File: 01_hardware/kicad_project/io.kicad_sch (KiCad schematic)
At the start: 24 parts, among them J5 ADDR HDR, J6 PROG PADS, J7 ARM SWD 10, SW1 DIP-6

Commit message: Rev E BOM: in-stock LCSC first source for every part; 2nd/3rd sources checked
- First sources swapped (same footprints, layout unchanged): U1 STM32G474RBT3,
  Q2/Q3/Q5/Q6 NCEP068N10G, 10k 0402 FOJAN, 100n 0402 merged onto C307331,
  1u 0402 CCTC, R62/R63/R89/R82, FB1 Murata BLM18KG601SN1D, L2/L3 cjiang
  FNR5040S470MT, C82 KEMET C0G (was X7R), RS1 Milliohm HoJLR2512, SS110 MDD
- LCSC part numbers for the hand-soldered headers (J1-J5, J7, JP1)
- Schematic and PCB fields, BOM, JLC BOM/CPL, PDFs and design notes regenerated;
  netlist check 0 errors, DRC unchanged
- BOM_sourcing_revE.xlsx: live LCSC stock 2026-10-20, 2nd/3rd sources checked
  for pinout / land pattern / ratings, PCB reserve options for T2 and U9

Co-Authored-By: Claude Opus 5.5 <noreply@anthropic.com>
Claude-Session: https://claude.ai/code/session_01A35wrnwFKLPSaRSxxHs471
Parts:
- J5: LCSC (none) -> C42419913; MPN ADDR HDR -> PZ254V-11-06P-A40
- J7: LCSC (none) -> C41376037; MPN FTSH-105-01-L-DV-K or equiv. -> HX PZ1.27-2x5P TP
- R32, R33, R34, R35, R36, R37: LCSC C25744 -> C2906861
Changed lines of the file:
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@@
       (effects (font (size 1.27 1.27)) hide)
     )
-    (property "LCSC" "C25744" (id 4) (at 129.54 71.12 0)
+    (property "LCSC" "C2906861" (id 4) (at 129.54 71.12 0)
       (effects (font (size 1.27 1.27)) hide)
     )
@@
       (effects (font (size 1.27 1.27)) hide)
     )
-    (property "LCSC" "C25744" (id 4) (at 116.84 71.12 0)
+    (property "LCSC" "C2906861" (id 4) (at 116.84 71.12 0)
       (effects (font (size 1.27 1.27)) hide)
     )
@@
       (effects (font (size 1.27 1.27)) hide)
     )
-    (property "LCSC" "C25744" (id 4) (at 104.14 71.12 0)
+    (property "LCSC" "C2906861" (id 4) (at 104.14 71.12 0)
       (effects (font (size 1.27 1.27)) hide)
     )
@@
       (effects (font (size 1.27 1.27)) hide)
     )
-    (property "LCSC" "C25744" (id 4) (at 91.44 71.12 0)
+    (property "LCSC" "C2906861" (id 4) (at 91.44 71.12 0)
       (effects (font (size 1.27 1.27)) hide)
     )
@@
       (effects (font (size 1.27 1.27)) hide)
     )
-    (property "LCSC" "C25744" (id 4) (at 78.74 71.12 0)
+    (property "LCSC" "C2906861" (id 4) (at 78.74 71.12 0)
       (effects (font (size 1.27 1.27)) hide)
     )
@@
       (effects (font (size 1.27 1.27)) hide)
     )
-    (property "LCSC" "C25744" (id 4) (at 66.04 71.12 0)
+    (property "LCSC" "C2906861" (id 4) (at 66.04 71.12 0)
       (effects (font (size 1.27 1.27)) hide)
     )
@@
       (effects (font (size 1.27 1.27)) hide)
     )
-    (property "LCSC" "" (id 4) (at 96.52 157.48 0)
-      (effects (font (size 1.27 1.27)) hide)
-    )
-    (property "MPN" "ADDR HDR" (id 5) (at 96.52 157.48 0)
+    (property "LCSC" "C42419913" (id 4) (at 96.52 157.48 0)
+      (effects (font (size 1.27 1.27)) hide)
+    )
+    (property "MPN" "PZ254V-11-06P-A40" (id 5) (at 96.52 157.48 0)
       (effects (font (size 1.27 1.27)) hide)
     )
@@
       (effects (font (size 1.27 1.27)) hide)
     )
-    (property "LCSC" "" (id 4) (at 228.6 180.34 0)
-      (effects (font (size 1.27 1.27)) hide)
-    )
-    (property "MPN" "FTSH-105-01-L-DV-K or equiv." (id 5) (at 228.6 180.34 0)
-      (effects (font (size 1.27 1.27)) hide)
-    )
+    (property "LCSC" "C41376037" (id 4) (at 228.6 180.34 0)
+      (effects (font (size 1.27 1.27)) hide)
+    )
+    (property "MPN" "HX PZ1.27-2x5P TP" (id 5) (at 228.6 180.34 0)
+      (effects (font (size 1.27 1.27)) hide)
+    )

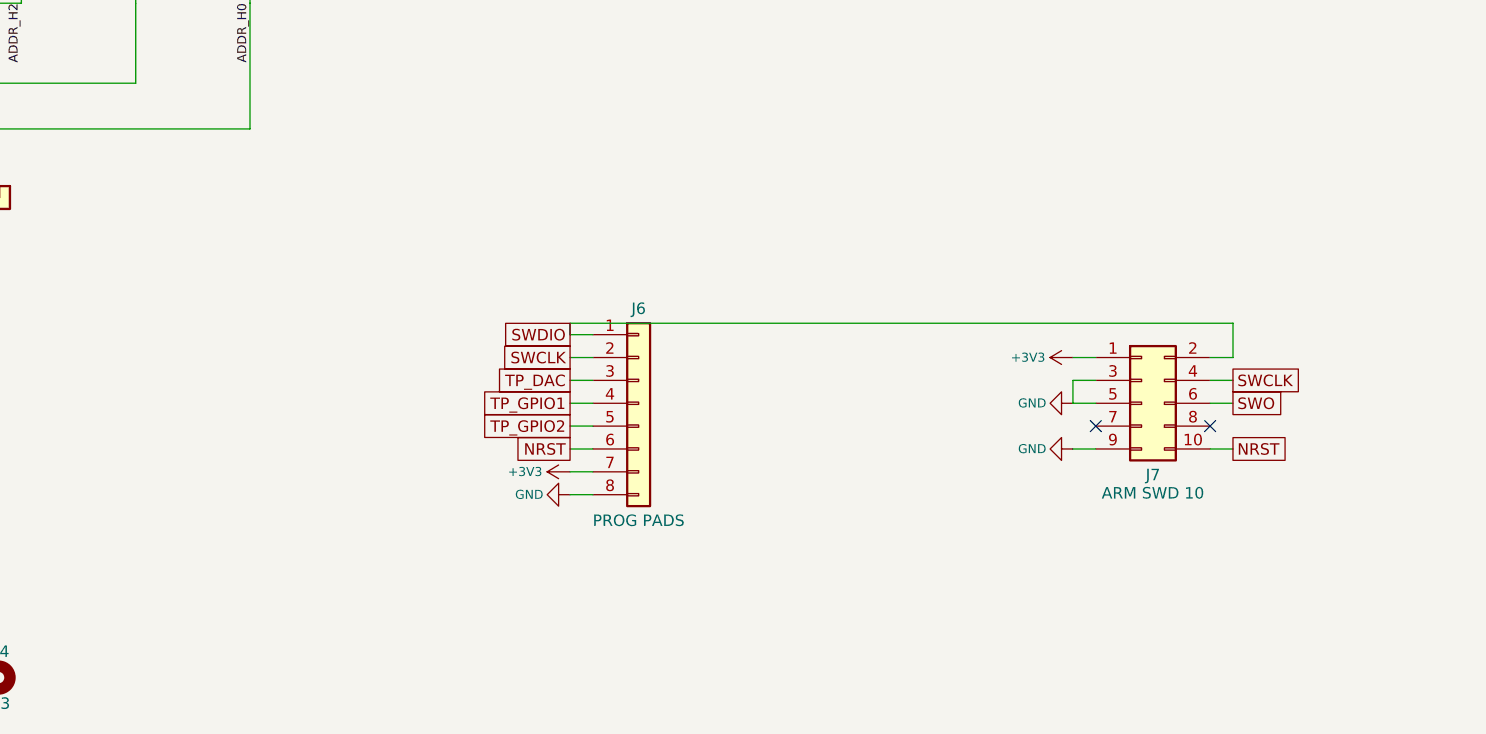
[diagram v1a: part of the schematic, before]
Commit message: Rev E2: debug-port series resistors, DRC clean (0 errors / 0 warnings)
- R123-R128 47.5 Ohm 0402 (C82290) in SWDIO, SWCLK, TP_DAC, TP_GPIO1,
  TP_GPIO2, NRST; R129 2 Ohm 0603 (C2933191) +3V3 -> J6.7 / J7 VTref
  (PROG_3V3). Placed on the MCU side of the J6/J7 branch, inserted into
  the existing traces.
- Cleared the 16 courtyard overlaps (T1/CR*/R64, T2/D8/C94/R116/C95/Q11/
  R114, C98/R122, C69/U11, C34/U1) with small moves, tracks re-attached;
  silk warnings gone. Parity 291 parts / 796 pads, 0 mismatches.
- BOMs, JLC BOM/CPL, gerbers, PDFs, EasyEDA zip, sourcing workbook,
  design notes, DRC report, README updated; scripts in 04_scripts/pcb6.

Co-Authored-By: Claude Opus 5.5 <noreply@anthropic.com>
Claude-Session: https://claude.ai/code/session_01A35wrnwFKLPSaRSxxHs471
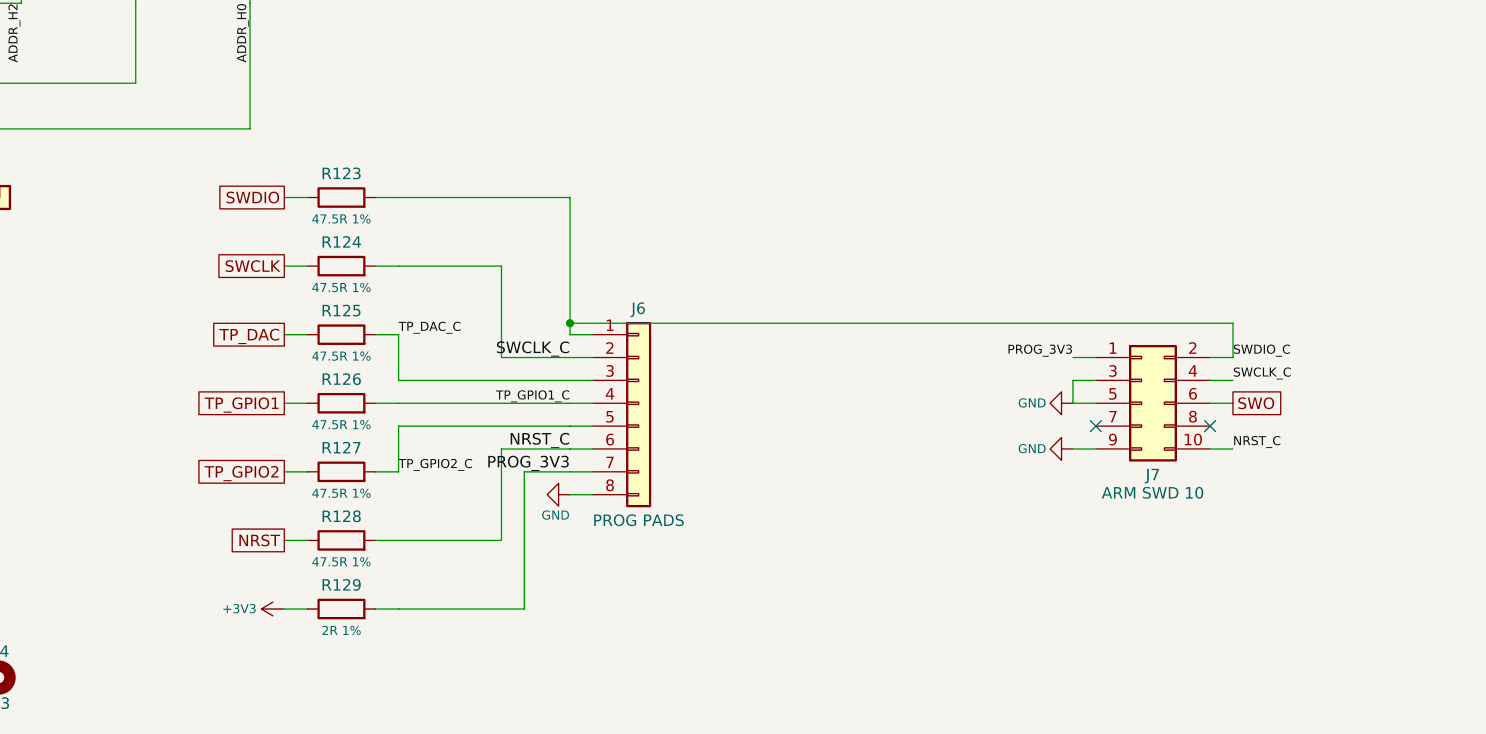
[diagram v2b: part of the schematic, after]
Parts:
- added R123, R124, R125, R126, R127, R128: 47.5R 1%, Resistor_SMD:R_0402_1005Metric, symbol Device:R
- added R129: 2R 1%, Resistor_SMD:R_0603_1608Metric, symbol Device:R
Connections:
- net +3V3: now also R129.1; no longer J6.7 (Pin_7), J7.1 (Pin_1)
- net NRST: now also R128.1; no longer J6.6 (Pin_6), J7.10 (Pin_10)
- net SWCLK: now also R124.1; no longer J6.2 (Pin_2), J7.4 (Pin_4)
- net SWDIO: now also R123.1; no longer J6.1 (Pin_1), J7.2 (Pin_2)
- net TP_DAC: now also R125.1; no longer J6.3 (Pin_3)
- net TP_GPIO1: now also R126.1; no longer J6.4 (Pin_4)
- net TP_GPIO2: now also R127.1; no longer J6.5 (Pin_5)
- new net NRST_C: J6.6 (Pin_6), J7.10 (Pin_10), R128.2
- new net PROG_3V3: J6.7 (Pin_7), J7.1 (Pin_1), R129.2
- new net SWCLK_C: J6.2 (Pin_2), J7.4 (Pin_4), R124.2
- new net SWDIO_C: J6.1 (Pin_1), J7.2 (Pin_2), R123.2
- new net TP_DAC_C: J6.3 (Pin_3), R125.2
- new net TP_GPIO1_C: J6.4 (Pin_4), R126.2
- new net TP_GPIO2_C: J6.5 (Pin_5), R127.2
